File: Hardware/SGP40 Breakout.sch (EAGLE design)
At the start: 24 parts, among them J2 QWIIC_RIGHT_ANGLE, J4 QWIIC_RIGHT_ANGLE, U1 SGP40

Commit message: Update logos on board
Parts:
- removed U$10, U$18: SPARKX-LOGO3, SparkX:SPARKX-LOGO3
- added LOGO2: QWIIC_LOGO_5MM, SparkFun-Aesthetics:QWIIC_LOGO_5MM
- added LOGO3, LOGO6: SFE_LOGO_NAME.1_INCH, SparkFun-Aesthetics:SFE_LOGO_NAME.1_INCH
- added LOGO4: SFE_LOGO_FLAME.1_INCH, SparkFun-Aesthetics:SFE_LOGO_FLAME.1_INCH
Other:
- note added: "Revised by: Priyanka Makin"
- note added: "v01"
- note removed: "X01"

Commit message: Petes updates:
Update version number in sch
Added 2 more standoffs (moved power LED and jumper)
Update value of qwiic connector in schematic
Update legacy vector font
Add qwiic connector and header measure
Switched I2C pullup resistors to 4.7k
Add min/max voltage of IC to sch
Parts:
- added JP7, JP8: STAND-OFF, SparkFun-Hardware:STAND-OFF
- J2, J4: value QWIIC_RIGHT_ANGLE -> QWIIC_RA
- R1, R2: value 10k -> 4.7k; device SparkFun-Resistors:10KOHM-0603-1/10W-1% -> SparkFun-Resistors:4.7KOHM-0603-1/10W-1%
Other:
- note added: "Abs min/max Vdd and Vddh: -0.3 to +3.6V"
- note added: "v10"
- note removed: "v01"
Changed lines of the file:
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@@
 <settings>
 <setting alwaysvectorfont="no"/>
-<setting keepoldvectorfont="yes"/>
 <setting verticaltext="up"/>
 </settings>
@@
 <part name="SUPPLY4" library="SparkFun-PowerSymbols" deviceset="3.3V" device=""/>
 <part name="GND4" library="SparkFun-PowerSymbols" deviceset="GND" device=""/>
-<part name="J2" library="SparkFun-Connectors" deviceset="QWIIC_CONNECTOR" device="JS-1MM" value="QWIIC_RIGHT_ANGLE"/>
+<part name="J2" library="SparkFun-Connectors" deviceset="QWIIC_CONNECTOR" device="JS-1MM" value="QWIIC_RA"/>
 <part name="GND6" library="SparkFun-PowerSymbols" deviceset="GND" device=""/>
 <part name="SUPPLY7" library="SparkFun-PowerSymbols" deviceset="3.3V" device=""/>
@@
 <part name="C4" library="SparkFun-Capacitors" deviceset="1.0UF" device="-0603-16V-10%-X7R" value="1.0uF"/>
 <part name="SUPPLY8" library="SparkFun-PowerSymbols" deviceset="3.3V" device=""/>
-<part name="J4" library="SparkFun-Connectors" deviceset="QWIIC_CONNECTOR" device="JS-1MM" value="QWIIC_RIGHT_ANGLE"/>
+<part name="J4" library="SparkFun-Connectors" deviceset="QWIIC_CONNECTOR" device="JS-1MM" value="QWIIC_RA"/>
 <part name="GND8" library="SparkFun-PowerSymbols" deviceset="GND" device=""/>
 <part name="JP1" library="SparkFun-Aesthetics" deviceset="FIDUCIAL" device="1X2"/>
@@
 <part name="GND3" library="SparkFun-PowerSymbols" deviceset="GND" device=""/>
 <part name="GND1" library="SparkFun-PowerSymbols" deviceset="GND" device=""/>
-<part name="R1" library="SparkFun-Resistors" deviceset="10KOHM" device="-0603-1/10W-1%" value="10k"/>
-<part name="R2" library="SparkFun-Resistors" deviceset="10KOHM" device="-0603-1/10W-1%" value="10k"/>
+<part name="R1" library="SparkFun-Resistors" deviceset="4.7KOHM" device="-0603-1/10W-1%" value="4.7k"/>
+<part name="R2" library="SparkFun-Resistors" deviceset="4.7KOHM" device="-0603-1/10W-1%" value="4.7k"/>
 <part name="SUPPLY9" library="SparkFun-PowerSymbols" deviceset="3.3V" device=""/>
 <part name="PWR" library="SparkFun-Jumpers" deviceset="JUMPER-SMT_2_NC_TRACE" device="_SILK" package3d_urn="urn:adsk.eagle:package:39281/1"/>
@@
 <part name="LOGO4" library="SparkFun-Aesthetics" deviceset="SFE_LOGO_FLAME" device=".1_INCH"/>
 <part name="LOGO6" library="SparkFun-Aesthetics" deviceset="SFE_LOGO_NAME" device=".1_INCH"/>
+<part name="JP7" library="SparkFun-Hardware" deviceset="STAND-OFF" device=""/>
+<part name="JP8" library="SparkFun-Hardware" deviceset="STAND-OFF" device=""/>
 </parts>
 <sheets>
@@
 <plain>
 <text x="165.862" y="11.43" size="2.54" layer="94" font="vector">Paul Clark</text>
-<text x="237.744" y="7.366" size="2.54" layer="94" font="vector">v01</text>
-<text x="121.92" y="78.74" size="1.778" layer="97" font="vector" align="center">7-bit unshifted I2C address: 0x59</text>
+<text x="237.744" y="7.366" size="2.54" layer="94" font="vector">v10</text>
+<text x="121.92" y="73.66" size="1.778" layer="97" font="vector" align="center">7-bit unshifted I2C address: 0x59</text>
 <text x="61.468" y="144.526" size="1.778" layer="97" font="vector">Power</text>
 <wire x1="0" y1="127" x2="121.92" y2="127" width="0.2032" layer="97" style="longdash"/>
@@
 <wire x1="121.92" y1="0" x2="121.92" y2="68.58" width="0.2032" layer="97" style="longdash"/>
 <text x="165.862" y="6.35" size="2.54" layer="94" font="vector">Revised by: Priyanka Makin</text>
+<text x="121.92" y="78.74" size="1.778" layer="97" font="vector" align="center">Abs min/max Vdd and Vddh: -0.3 to +3.6V</text>
 </plain>
 <instances>
@@
 <instance part="LOGO4" gate="G$1" x="213.36" y="38.1" smashed="yes"/>
 <instance part="LOGO6" gate="G$1" x="187.96" y="48.26" smashed="yes"/>
+<instance part="JP7" gate="G$1" x="243.84" y="30.48" smashed="yes"/>
+<instance part="JP8" gate="G$1" x="243.84" y="27.94" smashed="yes"/>
 </instances>
 <busses>

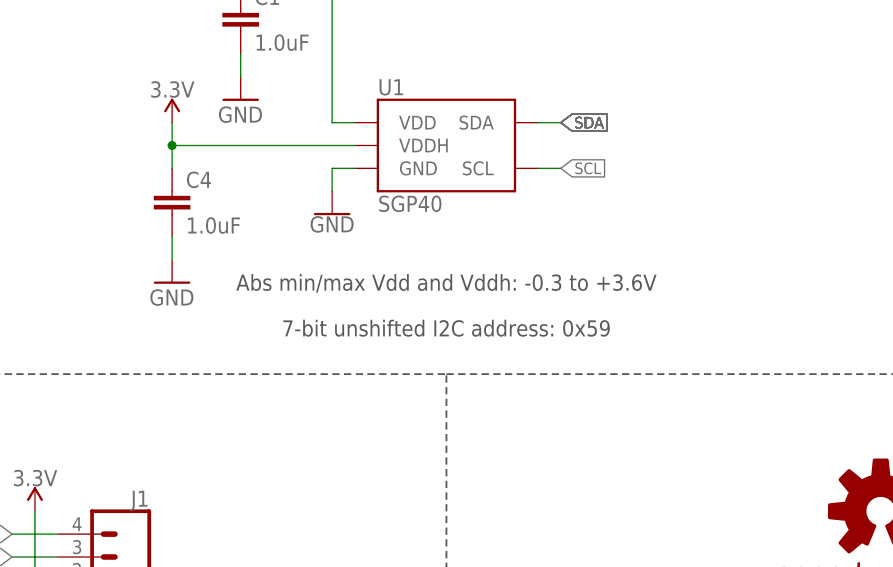
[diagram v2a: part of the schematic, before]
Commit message: Design review updates
SDA, SCL buzzard placement
3.3V trace → 20
Add operating current to sch
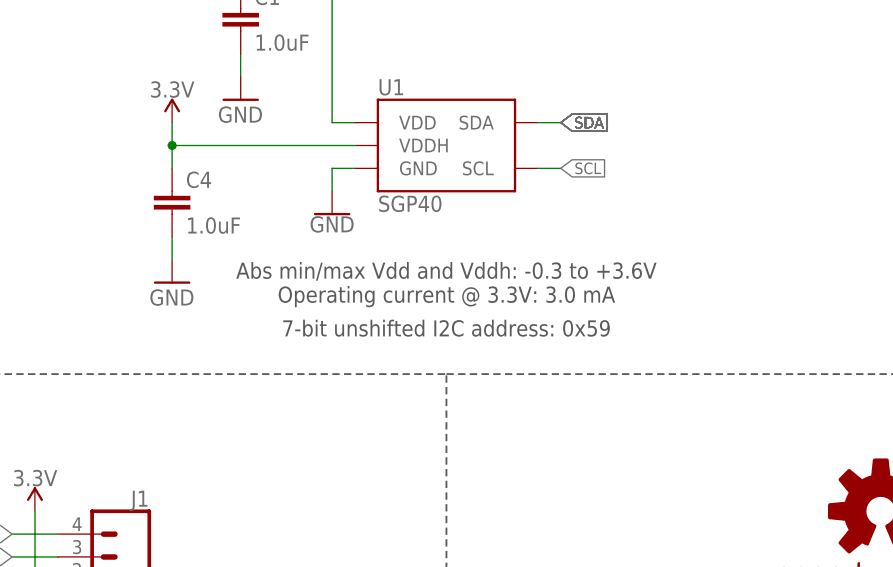
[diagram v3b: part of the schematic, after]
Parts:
- JP1, JP2, JP5, JP6: value FIDUCIAL1X2 -> FIDUCIAL0.2MM; device SparkFun-Aesthetics:FIDUCIAL1X2 -> SparkFun-Aesthetics:FIDUCIAL0.2MM
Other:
- note added: "Abs min/max Vdd and Vddh: -0.3 to +3.6V Operating current @ 3.3V: 3.0 mA"
- note removed: "Abs min/max Vdd and Vddh: -0.3 to +3.6V"
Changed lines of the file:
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@@
 <grid distance="0.1" unitdist="inch" unit="inch" style="lines" multiple="1" display="no" altdistance="0.01" altunitdist="inch" altunit="inch"/>
 <layers>
-<layer number="1" name="Top" color="4" fill="1" visible="yes" active="no"/>
-<layer number="2" name="Route2" color="1" fill="3" visible="yes" active="no"/>
-<layer number="3" name="Route3" color="4" fill="3" visible="yes" active="no"/>
-<layer number="4" name="Route4" color="1" fill="4" visible="yes" active="no"/>
-<layer number="5" name="Route5" color="4" fill="4" visible="yes" active="no"/>
-<layer number="6" name="Route6" color="1" fill="8" visible="yes" active="no"/>
-<layer number="7" name="Route7" color="4" fill="8" visible="yes" active="no"/>
-<layer number="8" name="Route8" color="1" fill="2" visible="yes" active="no"/>
-<layer number="9" name="Route9" color="4" fill="2" visible="yes" active="no"/>
-<layer number="10" name="Route10" color="1" fill="7" visible="yes" active="no"/>
-<layer number="11" name="Route11" color="4" fill="7" visible="yes" active="no"/>
-<layer number="12" name="Route12" color="1" fill="5" visible="yes" active="no"/>
-<layer number="13" name="Route13" color="4" fill="5" visible="yes" active="no"/>
-<layer number="14" name="Route14" color="1" fill="6" visible="yes" active="no"/>
-<layer number="15" name="Route15" color="4" fill="6" visible="yes" active="no"/>
-<layer number="16" name="Bottom" color="1" fill="1" visible="yes" active="no"/>
-<layer number="17" name="Pads" color="2" fill="1" visible="yes" active="no"/>
-<layer number="18" name="Vias" color="2" fill="1" visible="yes" active="no"/>
-<layer number="19" name="Unrouted" color="6" fill="1" visible="yes" active="no"/>
-<layer number="20" name="Dimension" color="24" fill="1" visible="yes" active="no"/>
-<layer number="21" name="tPlace" color="16" fill="1" visible="yes" active="no"/>
-<layer number="22" name="bPlace" color="14" fill="1" visible="yes" active="no"/>
-<layer number="23" name="tOrigins" color="15" fill="1" visible="yes" active="no"/>
-<layer number="24" name="bOrigins" color="15" fill="1" visible="yes" active="no"/>
-<layer number="25" name="tNames" color="7" fill="1" visible="yes" active="no"/>
-<layer number="26" name="bNames" color="7" fill="1" visible="yes" active="no"/>
-<layer number="27" name="tValues" color="7" fill="1" visible="yes" active="no"/>
-<layer number="28" name="bValues" color="7" fill="1" visible="yes" active="no"/>
+<layer number="1" name="Top" color="4" fill="1" visible="no" active="no"/>
+<layer number="2" name="Route2" color="1" fill="3" visible="no" active="no"/>
+<layer number="3" name="Route3" color="4" fill="3" visible="no" active="no"/>
+<layer number="4" name="Route4" color="1" fill="4" visible="no" active="no"/>
+<layer number="5" name="Route5" color="4" fill="4" visible="no" active="no"/>
+<layer number="6" name="Route6" color="1" fill="8" visible="no" active="no"/>
+<layer number="7" name="Route7" color="4" fill="8" visible="no" active="no"/>
+<layer number="8" name="Route8" color="1" fill="2" visible="no" active="no"/>
+<layer number="9" name="Route9" color="4" fill="2" visible="no" active="no"/>
+<layer number="10" name="Route10" color="1" fill="7" visible="no" active="no"/>
+<layer number="11" name="Route11" color="4" fill="7" visible="no" active="no"/>
+<layer number="12" name="Route12" color="1" fill="5" visible="no" active="no"/>
+<layer number="13" name="Route13" color="4" fill="5" visible="no" active="no"/>
+<layer number="14" name="Route14" color="1" fill="6" visible="no" active="no"/>
+<layer number="15" name="Route15" color="4" fill="6" visible="no" active="no"/>
+<layer number="16" name="Bottom" color="1" fill="1" visible="no" active="no"/>
+<layer number="17" name="Pads" color="2" fill="1" visible="no" active="no"/>
+<layer number="18" name="Vias" color="2" fill="1" visible="no" active="no"/>
+<layer number="19" name="Unrouted" color="6" fill="1" visible="no" active="no"/>
+<layer number="20" name="Dimension" color="24" fill="1" visible="no" active="no"/>
+<layer number="21" name="tPlace" color="16" fill="1" visible="no" active="no"/>
+<layer number="22" name="bPlace" color="14" fill="1" visible="no" active="no"/>
+<layer number="23" name="tOrigins" color="15" fill="1" visible="no" active="no"/>
+<layer number="24" name="bOrigins" color="15" fill="1" visible="no" active="no"/>
+<layer number="25" name="tNames" color="7" fill="1" visible="no" active="no"/>
+<layer number="26" name="bNames" color="7" fill="1" visible="no" active="no"/>
+<layer number="27" name="tValues" color="7" fill="1" visible="no" active="no"/>
+<layer number="28" name="bValues" color="7" fill="1" visible="no" active="no"/>
 <layer number="29" name="tStop" color="7" fill="3" visible="no" active="no"/>
 <layer number="30" name="bStop" color="7" fill="6" visible="no" active="no"/>
@@
 <layer number="35" name="tGlue" color="7" fill="4" visible="no" active="no"/>
 <layer number="36" name="bGlue" color="7" fill="5" visible="no" active="no"/>
-<layer number="37" name="tTest" color="7" fill="1" visible="yes" active="no"/>
-<layer number="38" name="bTest" color="7" fill="1" visible="yes" active="no"/>
+<layer number="37" name="tTest" color="7" fill="1" visible="no" active="no"/>
+<layer number="38" name="bTest" color="7" fill="1" visible="no" active="no"/>
 <layer number="39" name="tKeepout" color="4" fill="11" visible="no" active="no"/>
 <layer number="40" name="bKeepout" color="1" fill="11" visible="no" active="no"/>
@@
 <layer number="44" name="Drills" color="7" fill="1" visible="no" active="no"/>
 <layer number="45" name="Holes" color="7" fill="1" visible="no" active="no"/>
-<layer number="46" name="Milling" color="3" fill="1" visible="yes" active="no"/>
-<layer number="47" name="Measures" color="7" fill="1" visible="yes" active="no"/>
-<layer number="48" name="Document" color="7" fill="1" visible="yes" active="no"/>
-<layer number="49" name="Reference" color="7" fill="1" visible="yes" active="no"/>
-<layer number="50" name="dxf" color="7" fill="1" visible="yes" active="no"/>
-<layer number="51" name="tDocu" color="6" fill="1" visible="yes" active="no"/>
-<layer number="52" name="bDocu" color="7" fill="1" visible="yes" active="no"/>
-<layer number="53" name="tGND_GNDA" color="7" fill="9" visible="yes" active="no"/>
-<layer number="54" name="bGND_GNDA" color="1" fill="9" visible="yes" active="no"/>
-<layer number="56" name="wert" color="7" fill="1" visible="yes" active="no"/>
-<layer number="57" name="tCAD" color="7" fill="1" visible="yes" active="no"/>
-<layer number="59" name="tCarbon" color="7" fill="1" visible="yes" active="no"/>
-<layer number="60" name="bCarbon" color="7" fill="1" visible="yes" active="no"/>
+<layer number="46" name="Milling" color="3" fill="1" visible="no" active="no"/>
+<layer number="47" name="Measures" color="7" fill="1" visible="no" active="no"/>
+<layer number="48" name="Document" color="7" fill="1" visible="no" active="no"/>
+<layer number="49" name="Reference" color="7" fill="1" visible="no" active="no"/>
+<layer number="50" name="dxf" color="7" fill="1" visible="no" active="no"/>
+<layer number="51" name="tDocu" color="6" fill="1" visible="no" active="no"/>
+<layer number="52" name="bDocu" color="7" fill="1" visible="no" active="no"/>
+<layer number="53" name="tGND_GNDA" color="7" fill="9" visible="no" active="no"/>
+<layer number="54" name="bGND_GNDA" color="1" fill="9" visible="no" active="no"/>
+<layer number="56" name="wert" color="7" fill="1" visible="no" active="no"/>
+<layer number="57" name="tCAD" color="7" fill="1" visible="no" active="no"/>
+<layer number="59" name="tCarbon" color="7" fill="1" visible="no" active="no"/>
+<layer number="60" name="bCarbon" color="7" fill="1" visible="no" active="no"/>
 <layer number="88" name="SimResults" color="9" fill="1" visible="no" active="yes"/>
 <layer number="89" name="SimProbes" color="9" fill="1" visible="no" active="yes"/>
@@
 <part name="JP3" library="SparkFun-Hardware" deviceset="STAND-OFF" device=""/>
 <part name="JP4" library="SparkFun-Hardware" deviceset="STAND-OFF" device=""/>
-<part name="JP2" library="SparkFun-Aesthetics" deviceset="FIDUCIAL" device="1X2"/>
-<part name="JP6" library="SparkFun-Aesthetics" deviceset="FIDUCIAL" device="1X2"/>
+<part name="JP2" library="SparkFun-Aesthetics" deviceset="FIDUCIAL" device="0.2MM" value="FIDUCIAL0.2MM"/>
+<part name="JP6" library="SparkFun-Aesthetics" deviceset="FIDUCIAL" device="0.2MM" value="FIDUCIAL0.2MM"/>
 <part name="SUPPLY4" library="SparkFun-PowerSymbols" deviceset="3.3V" device=""/>
 <part name="GND4" library="SparkFun-PowerSymbols" deviceset="GND" device=""/>
@@
 <part name="J4" library="SparkFun-Connectors" deviceset="QWIIC_CONNECTOR" device="JS-1MM" value="QWIIC_RA"/>
 <part name="GND8" library="SparkFun-PowerSymbols" deviceset="GND" device=""/>
-<part name="JP1" library="SparkFun-Aesthetics" deviceset="FIDUCIAL" device="1X2"/>
-<part name="JP5" library="SparkFun-Aesthetics" deviceset="FIDUCIAL" device="1X2"/>
+<part name="JP1" library="SparkFun-Aesthetics" deviceset="FIDUCIAL" device="0.2MM" value="FIDUCIAL0.2MM"/>
+<part name="JP5" library="SparkFun-Aesthetics" deviceset="FIDUCIAL" device="0.2MM" value="FIDUCIAL0.2MM"/>
 <part name="R3" library="SparkFun-Resistors" deviceset="1KOHM" device="-0603-1/10W-1%" value="1k"/>
 <part name="SUPPLY10" library="SparkFun-PowerSymbols" deviceset="3.3V" device=""/>
@@
 <wire x1="121.92" y1="0" x2="121.92" y2="68.58" width="0.2032" layer="97" style="longdash"/>
 <text x="165.862" y="6.35" size="2.54" layer="94" font="vector">Revised by: Priyanka Makin</text>
-<text x="121.92" y="78.74" size="1.778" layer="97" font="vector" align="center">Abs min/max Vdd and Vddh: -0.3 to +3.6V</text>
+<text x="121.92" y="78.74" size="1.778" layer="97" font="vector" align="center">Abs min/max Vdd and Vddh: -0.3 to +3.6V
+Operating current @ 3.3V: 3.0 mA</text>
 </plain>
 <instances>

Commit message: QC Double-check
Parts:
- J1: value (none) -> DNP
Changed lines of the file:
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@@
 <part name="PWR" library="SparkFun-Jumpers" deviceset="JUMPER-SMT_2_NC_TRACE" device="_SILK" package3d_urn="urn:adsk.eagle:package:39281/1"/>
 <part name="LOGO5" library="SparkFun-Aesthetics" deviceset="OSHW-LOGO" device="S"/>
-<part name="J1" library="SparkFun-Connectors" deviceset="CONN_04" device="1X04_NO_SILK"/>
+<part name="J1" library="SparkFun-Connectors" deviceset="CONN_04" device="1X04_NO_SILK" value="DNP"/>
 <part name="I2C" library="SparkFun-Jumpers" deviceset="JUMPER-SMT_3_2-NC_TRACE" device="_SILK" package3d_urn="urn:adsk.eagle:package:39289/1"/>
 <part name="SUPPLY1" library="SparkFun-PowerSymbols" deviceset="3.3V" device=""/>
@@
 </instance>
 <instance part="GND1" gate="1" x="109.22" y="86.36" smashed="yes">
-<attribute name="VALUE" x="109.22" y="86.106" size="1.778" layer="96" font="vector" align="top-center"/>
+<attribute name="VALUE" x="106.68" y="83.566" size="1.778" layer="96" font="vector"/>
 </instance>
 <instance part="R1" gate="G$1" x="177.8" y="154.94" smashed="yes" rot="R90">
